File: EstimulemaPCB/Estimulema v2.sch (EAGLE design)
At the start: 159 parts, among them IC3 74AC14N, IC4 ISO7240S, J1 JUMPERS12MM, J2 J15MM, J3 J_7MM, J4 JUMPERS5MM, J5 JUMPERS7MM, J6 J7MM, K2 HC-06, Q17 TIP48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

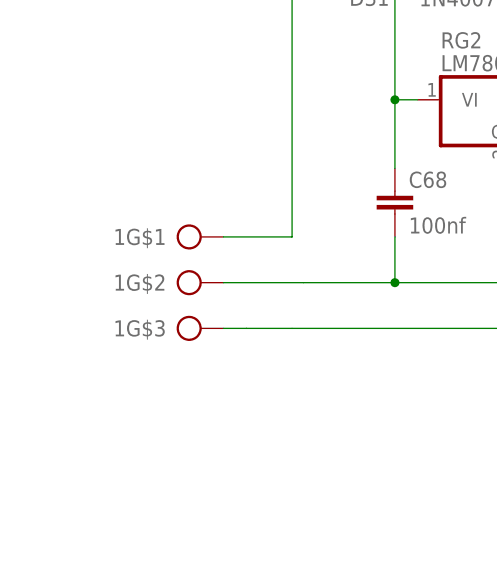
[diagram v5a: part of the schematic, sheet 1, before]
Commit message: update pcb y ino para teste calibracion dac
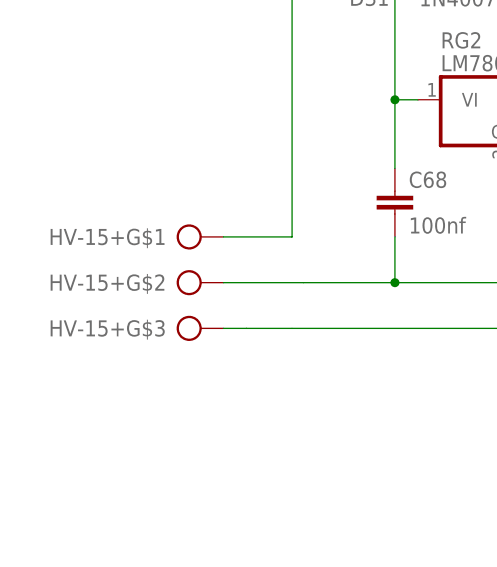
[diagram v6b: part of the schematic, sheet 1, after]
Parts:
- HV-15+: value PTR500 -> CONECTOR_3_PTR500
- R22: value 4K7 -> 470R
- renumbered 1 to HV-15+
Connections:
- net N$67 renamed RL1
- net N$68 renamed RL2
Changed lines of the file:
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@@
 <?xml version="1.0" encoding="utf-8"?>
 <!DOCTYPE eagle SYSTEM "eagle.dtd">
-<eagle version="9.2.1">
+<eagle version="9.2.2">
 <drawing>
 <settings>
@@
 <setting verticaltext="up"/>
 </settings>
-<grid distance="10" unitdist="mil" unit="mil" style="lines" multiple="1" display="no" altdistance="0.01" altunitdist="inch" altunit="inch"/>
+<grid distance="0.1" unitdist="inch" unit="inch" style="lines" multiple="1" display="no" altdistance="0.01" altunitdist="inch" altunit="inch"/>
 <layers>
 <layer number="1" name="Top" color="4" fill="1" visible="no" active="no"/>
@@
 <part name="SG2" library="7DI Library" library_urn="urn:adsk.eagle:library:1229688" deviceset="BUZZER" device="" package3d_urn="urn:adsk.eagle:package:1734311/2"/>
 <part name="LED3" library="7DI Library" library_urn="urn:adsk.eagle:library:1229688" deviceset="LED" device="LED_T_3MM" package3d_urn="urn:adsk.eagle:package:1238520/2" value="LEDLED_T_3MM"/>
-<part name="R22" library="7DI Library" library_urn="urn:adsk.eagle:library:1229688" deviceset="RESISTOR" device="SMD_0805" package3d_urn="urn:adsk.eagle:package:1282003/2" value="4K7"/>
+<part name="R22" library="7DI Library" library_urn="urn:adsk.eagle:library:1229688" deviceset="RESISTOR" device="SMD_0805" package3d_urn="urn:adsk.eagle:package:1282003/2" value="470R"/>
 <part name="D2" library="7DI Library" library_urn="urn:adsk.eagle:library:1229688" deviceset="DIODO" device="WEB" package3d_urn="urn:adsk.eagle:package:4574534/2" value="1N4007S"/>
 <part name="R23" library="7DI Library" library_urn="urn:adsk.eagle:library:1229688" deviceset="RESISTOR" device="SMD_0805" package3d_urn="urn:adsk.eagle:package:1282003/2" value="120R"/>
@@
 <part name="R19" library="7DI Library" library_urn="urn:adsk.eagle:library:1229688" deviceset="RESISTOR" device="SMD_0805" package3d_urn="urn:adsk.eagle:package:1282003/2" value="820r"/>
 <part name="R27" library="7DI Library" library_urn="urn:adsk.eagle:library:1229688" deviceset="RESISTOR" device="SMD_0805" package3d_urn="urn:adsk.eagle:package:1282003/2" value="820R"/>
-<part name="X1HV+" library="7DI Library" library_urn="urn:adsk.eagle:library:1229688" deviceset="CONECTOR_" device="5.08" package3d_urn="urn:adsk.eagle:package:1393551/4"/>
-<part name="X3HV-" library="7DI Library" library_urn="urn:adsk.eagle:library:1229688" deviceset="CONECTOR_" device="5.08" package3d_urn="urn:adsk.eagle:package:1393551/4"/>
+<part name="X1HV+" library="7DI Library" library_urn="urn:adsk.eagle:library:1229688" deviceset="CONECTOR_" device="5.08" package3d_urn="urn:adsk.eagle:package:1393551/4" value=""/>
+<part name="X3HV-" library="7DI Library" library_urn="urn:adsk.eagle:library:1229688" deviceset="CONECTOR_" device="5.08" package3d_urn="urn:adsk.eagle:package:1393551/4" value=""/>
 <part name="X2+15-" library="7DI Library" library_urn="urn:adsk.eagle:library:1229688" deviceset="CONECTOR_" device="5.08" package3d_urn="urn:adsk.eagle:package:1393551/4"/>
 <part name="JP11" library="pinhead" library_urn="urn:adsk.eagle:library:325" deviceset="PINHD-1X7" device="" package3d_urn="urn:adsk.eagle:package:22477/2"/>
@@
 <part name="UART_COM" library="pinhead" library_urn="urn:adsk.eagle:library:325" deviceset="PINHD-2X2" device="" package3d_urn="urn:adsk.eagle:package:22455/2"/>
 <part name="GPIO2_ACCEL" library="pinhead" library_urn="urn:adsk.eagle:library:325" deviceset="PINHD-1X4" device="" package3d_urn="urn:adsk.eagle:package:22407/2"/>
-<part name="1" library="7DI Library" library_urn="urn:adsk.eagle:library:1229688" deviceset="CONECTOR_3_PTR500" device="" package3d_urn="urn:adsk.eagle:package:5402944/3" value="PTR500"/>
+<part name="HV-15+" library="7DI Library" library_urn="urn:adsk.eagle:library:1229688" deviceset="CONECTOR_3_PTR500" device="" package3d_urn="urn:adsk.eagle:package:5402944/3" value=""/>
 </parts>
 <sheets>
@@
 <attribute name="VALUE" x="124.46" y="43.18" size="1.778" layer="96"/>
 </instance>
-<instance part="1" gate="G$1" x="-114.3" y="25.4" smashed="yes">
+<instance part="HV-15+" gate="G$1" x="-114.3" y="25.4" smashed="yes">
 <attribute name="NAME" x="-115.57" y="26.289" size="1.778" layer="95" rot="R180"/>
 </instance>
-<instance part="1" gate="G$2" x="-114.3" y="20.32" smashed="yes">
+<instance part="HV-15+" gate="G$2" x="-114.3" y="20.32" smashed="yes">
 <attribute name="NAME" x="-115.57" y="21.209" size="1.778" layer="95" rot="R180"/>
 </instance>
-<instance part="1" gate="G$3" x="-114.3" y="15.24" smashed="yes">
+<instance part="HV-15+" gate="G$3" x="-114.3" y="15.24" smashed="yes">
 <attribute name="NAME" x="-115.57" y="16.129" size="1.778" layer="95" rot="R180"/>
 </instance>
@@
 <wire x1="0" y1="27.94" x2="-8.89" y2="27.94" width="0.1524" layer="91"/>
 <junction x="-8.89" y="27.94"/>
-<pinref part="1" gate="G$1" pin="KL"/>
+<pinref part="HV-15+" gate="G$1" pin="KL"/>
 <wire x1="-109.22" y1="25.4" x2="-101.6" y2="25.4" width="0.1524" layer="91"/>
 </segment>
@@
 <wire x1="0" y1="15.24" x2="-8.89" y2="15.24" width="0.1524" layer="91"/>
 <junction x="-8.89" y="15.24"/>
-<pinref part="1" gate="G$2" pin="KL"/>
+<pinref part="HV-15+" gate="G$2" pin="KL"/>
 <wire x1="-109.22" y1="20.32" x2="-100.33" y2="20.32" width="0.1524" layer="91"/>
 </segment>
@@
 <wire x1="-101.6" y1="15.24" x2="-67.31" y2="15.24" width="0.1524" layer="91"/>
 <wire x1="-35.56" y1="15.24" x2="-67.31" y2="15.24" width="0.1524" layer="91"/>
-<pinref part="1" gate="G$3" pin="KL"/>
+<pinref part="HV-15+" gate="G$3" pin="KL"/>
 <wire x1="-109.22" y1="15.24" x2="-106.68" y2="15.24" width="0.1524" layer="91"/>
 <wire x1="-106.68" y1="15.24" x2="-101.6" y2="15.24" width="0.1524" layer="91"/>
@@
 </segment>
 </net>
-<net name="N$67" class="2">
+<net name="RL1" class="2">
 <segment>
 <pinref part="UC1" gate="G$1" pin="6/PWM"/>
@@
 </segment>
 </net>
-<net name="N$68" class="2">
+<net name="RL2" class="2">
 <segment>
 <pinref part="UC1" gate="G$1" pin="7/RX3"/>
